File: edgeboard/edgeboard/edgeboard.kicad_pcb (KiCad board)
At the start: 2 copper layers, 117.2 x 150.2 mm, 26 parts

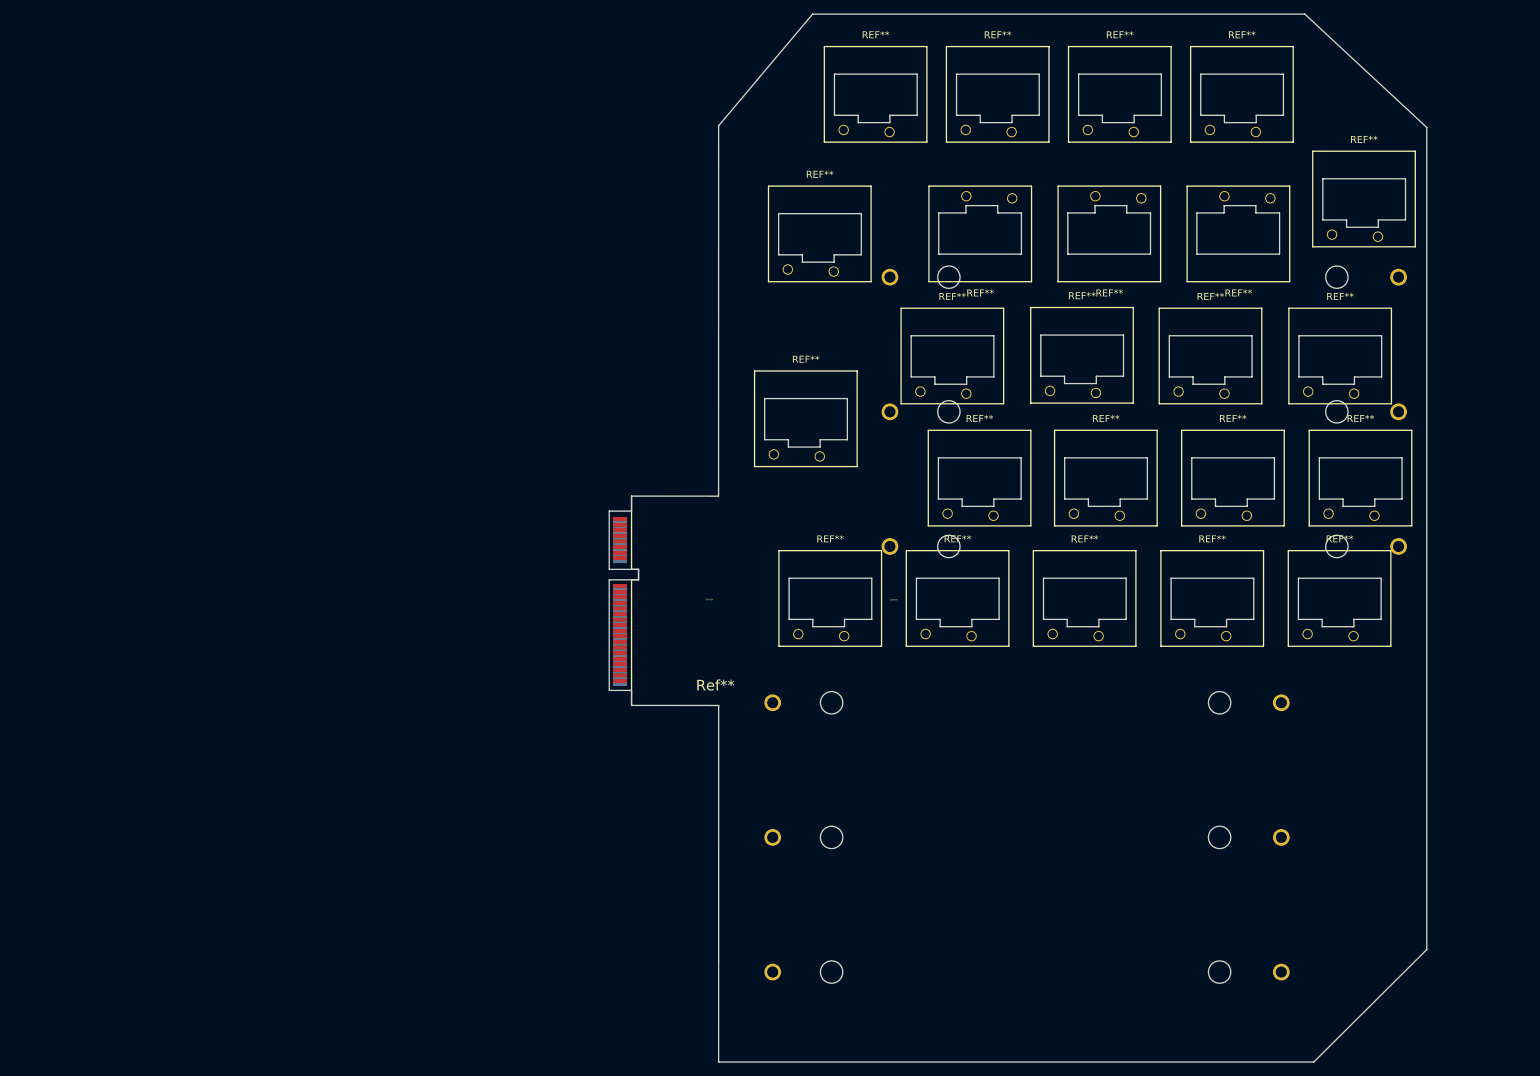
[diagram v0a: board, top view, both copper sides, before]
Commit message: added USB-C
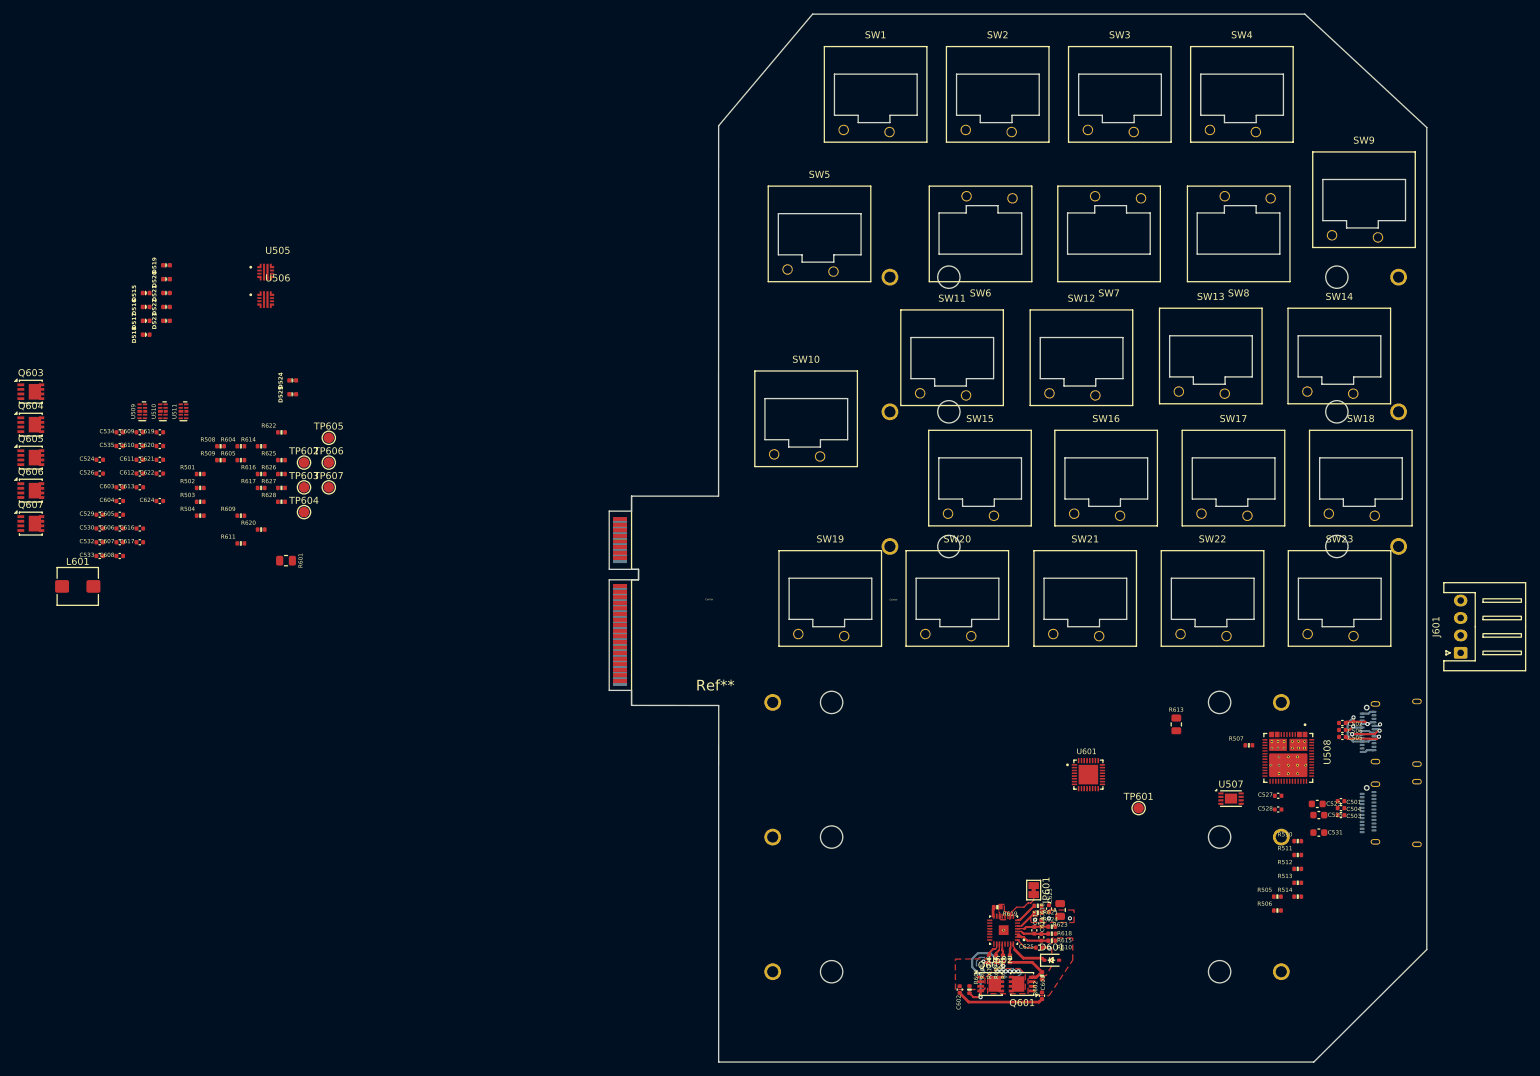
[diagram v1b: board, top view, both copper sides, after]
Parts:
- removed REF** (x16): SW_Kailh_Choc_Mini_1.00u, PCM_Switch_Keyboard_Kailh:SW_Kailh_Choc_Mini_1.00u
- removed REF** (x4): SW_Kailh_Choc_Mini_1.25u_90deg, PCM_Switch_Keyboard_Kailh:SW_Kailh_Choc_Mini_1.25u_90deg
- removed REF**: SW_Kailh_Choc_Mini_1.50u, PCM_Switch_Keyboard_Kailh:SW_Kailh_Choc_Mini_1.50u
- removed REF**: SW_Kailh_Choc_Mini_1.50u_90deg, PCM_Switch_Keyboard_Kailh:SW_Kailh_Choc_Mini_1.50u_90deg
- removed REF** (x2): BAT_BK-18650-PC6, keyswitch:BAT_BK-18650-PC6
- removed REF**: SW_Kailh_Choc_Mini_ISOEnter_180deg, PCM_Switch_Keyboard_Kailh:SW_Kailh_Choc_Mini_ISOEnter_180deg
- added BT1: BK-18650-PC6, keyswitch:BAT_BK-18650-PC6, B.Cu at (214.8, 69.0)
- added BT2: BK-18650-PC6, keyswitch:BAT_BK-18650-PC6, B.Cu at (198.0, 129.9)
- added C501: 100nF/50V, A_HDJ_Library:C_0402_1005Metric, F.Cu at (243.2, 124.8)
- added C502: 100nF/50V, A_HDJ_Library:C_0402_1005Metric, F.Cu at (243.4, 113.6)
- added C503: 47pF, A_HDJ_Library:C_0402_1005Metric, F.Cu at (243.2, 126.8)
- added C504: 47pF, A_HDJ_Library:C_0402_1005Metric, F.Cu at (243.2, 125.8)
- added C505: 47pF, A_HDJ_Library:C_0402_1005Metric, F.Cu at (243.4, 115.6)
- added C506: 47pF, A_HDJ_Library:C_0402_1005Metric, F.Cu at (243.4, 114.6)
- added C523: 22uF/10V, A_HDJ_Library:C_0603_1608Metric, F.Cu at (239.8, 125.2)
- added C524: 100nF/50V, A_HDJ_Library:C_0402_1005Metric, F.Cu at (65.3, 75.9)
- added C525: 10uF/10V, A_HDJ_Library:C_0603_1608Metric, F.Cu at (240.0, 126.8)
- added C526: 100nF/50V, A_HDJ_Library:C_0402_1005Metric, F.Cu at (65.3, 77.8)
- added C527: 100nF/50V, A_HDJ_Library:C_0402_1005Metric, F.Cu at (234.2, 124.0)
- added C528: 4.7uF/10V, A_HDJ_Library:C_0402_1005Metric, F.Cu at (234.2, 126.0)
- added C529: 47pF/50V, A_HDJ_Library:C_0402_1005Metric, F.Cu at (65.3, 83.8)
- added C530: 47pF/50V, A_HDJ_Library:C_0402_1005Metric, F.Cu at (65.3, 85.7)
- added C531: 10uF/10V, A_HDJ_Library:C_0603_1608Metric, F.Cu at (240.0, 129.3)
- added C532: 100nF/50V, A_HDJ_Library:C_0402_1005Metric, F.Cu at (65.3, 87.7)
- added C533: 100nF/50V, A_HDJ_Library:C_0402_1005Metric, F.Cu at (65.3, 89.7)
- added C534: 47pF/50V, A_HDJ_Library:C_0402_1005Metric, F.Cu at (68.2, 71.9)
- added C535: 47pF/50V, A_HDJ_Library:C_0402_1005Metric, F.Cu at (68.2, 73.9)
- added C601: 0.1u, A_HDJ_Library:C_0402_1005Metric, F.Cu at (200.3, 152.7)
- added C602: 0.1u, A_HDJ_Library:C_0402_1005Metric, F.Cu at (188.6, 151.8)
- added C603: 3x10uF MLCC, A_HDJ_Library:C_0402_1005Metric, F.Cu at (68.2, 79.8)
- added C604: 47n, A_HDJ_Library:C_0402_1005Metric, F.Cu at (68.2, 81.8)
- added C605: 47n, A_HDJ_Library:C_0402_1005Metric, F.Cu at (68.2, 83.8)
- added C606: 10uF MLCC, A_HDJ_Library:C_0402_1005Metric, F.Cu at (68.2, 85.7)
- added C607: 10uF MLCC, A_HDJ_Library:C_0402_1005Metric, F.Cu at (68.2, 87.7)
- added C608: 10uF MLCC, A_HDJ_Library:C_0402_1005Metric, F.Cu at (68.2, 89.7)
- added C609: 10uF MLCC, A_HDJ_Library:C_0402_1005Metric, F.Cu at (71.0, 71.9)
- added C610: 33n, A_HDJ_Library:C_0402_1005Metric, F.Cu at (71.0, 73.9)
- added C611: 33n, A_HDJ_Library:C_0402_1005Metric, F.Cu at (71.0, 75.9)
- added C612: 0.47u, A_HDJ_Library:C_0402_1005Metric, F.Cu at (71.0, 77.8)
- added C613: 0.1u, A_HDJ_Library:C_0402_1005Metric, F.Cu at (71.0, 79.8)
- added C614: 0.1u, A_HDJ_Library:C_0402_1005Metric, F.Cu at (200.2, 144.3)
- added C615: 0.1u, A_HDJ_Library:C_0402_1005Metric, F.Cu at (199.2, 143.3)
- added C616: 33p, A_HDJ_Library:C_0402_1005Metric, F.Cu at (71.0, 85.7)
- added C617: 1800p, A_HDJ_Library:C_0402_1005Metric, F.Cu at (71.0, 87.7)
- added C618: 0.1u, A_HDJ_Library:C_0402_1005Metric, F.Cu at (200.2, 142.3)
- added C619: 1u, A_HDJ_Library:C_0402_1005Metric, F.Cu at (73.9, 71.9)
- added C620: 2.2u, A_HDJ_Library:C_0402_1005Metric, F.Cu at (73.9, 73.9)
- added C621: 15p, A_HDJ_Library:C_0402_1005Metric, F.Cu at (73.9, 75.9)
- added C622: 680p, A_HDJ_Library:C_0402_1005Metric, F.Cu at (73.9, 77.8)
- added C623: 0.1u, A_HDJ_Library:C_0402_1005Metric, F.Cu at (201.3, 140.2)
- added C624: 100p, A_HDJ_Library:C_0402_1005Metric, F.Cu at (73.9, 81.8)
- added C625: 2.2u, A_HDJ_Library:C_0402_1005Metric, F.Cu at (199.9, 145.8)
- added D515: ESD9B3.3ST5GOSCT-ND, A_HDJ_Library:D_0402_1005Metric, F.Cu at (72.0, 52.0)
- added D516: ESD9B3.3ST5GOSCT-ND, A_HDJ_Library:D_0402_1005Metric, F.Cu at (72.0, 54.0)
- added D517: ESD9B3.3ST5GOSCT-ND, A_HDJ_Library:D_0402_1005Metric, F.Cu at (72.0, 56.0)
- added D518: ESD9B3.3ST5GOSCT-ND, A_HDJ_Library:D_0402_1005Metric, F.Cu at (72.0, 57.9)
- added D519: ESD9B3.3ST5GOSCT-ND, A_HDJ_Library:D_0402_1005Metric, F.Cu at (74.9, 48.0)
- added D520: ESD9B3.3ST5GOSCT-ND, A_HDJ_Library:D_0402_1005Metric, F.Cu at (74.9, 50.0)
- added D521: ESD9B3.3ST5GOSCT-ND, A_HDJ_Library:D_0402_1005Metric, F.Cu at (74.9, 52.0)
- added D522: ESD9B3.3ST5GOSCT-ND, A_HDJ_Library:D_0402_1005Metric, F.Cu at (74.9, 54.0)
- added D523: ESD9B3.3ST5GOSCT-ND, A_HDJ_Library:D_0402_1005Metric, F.Cu at (74.9, 56.0)
- added D524: ESD9B3.3ST5GOSCT-ND, A_HDJ_Library:D_0402_1005Metric, F.Cu at (93.0, 64.5)
- added D525: ESD9B3.3ST5GOSCT-ND, A_HDJ_Library:D_0402_1005Metric, F.Cu at (93.0, 66.5)
- added D601: BAT54HT1, A_HDJ_Library:D_SOD-323, F.Cu at (201.8, 147.6)
- added J501: USB_C_Receptacle, Connector_USB:USB_C_Receptacle_Amphenol_12401610E4-2A, B.Cu at (251.2, 126.5)
- added J502: USB_C_Receptacle, Connector_USB:USB_C_Receptacle_Amphenol_12401610E4-2A, B.Cu at (251.2, 115.0)
- added J601: JST XH 4 pin, Connector_JST:JST_XH_S4B-XH-A_1x04_P2.50mm_Horizontal, F.Cu at (260.4, 103.5)
- added JP601: Jumper_2_Bridged, Jumper:SolderJumper-2_P1.3mm_Bridged_Pad1.0x1.5mm, F.Cu at (199.2, 137.6)
- added L601: 2.2uH 4.5A+, Inductor_SMD:L_Bourns_SRP5030T, F.Cu at (62.1, 94.0)
- added Q601: CSD17551Q3A, Package_SO:Vishay_PowerPAK_1212-8_Single, F.Cu at (197.5, 151.0)
- added Q602: CSD17551Q3A, Package_SO:Vishay_PowerPAK_1212-8_Single, F.Cu at (193.0, 151.0)
- added Q603: CSD17551Q3A, Package_SO:Vishay_PowerPAK_1212-8_Single, F.Cu at (55.4, 66.1)
- added Q604: CSD17551Q3A, Package_SO:Vishay_PowerPAK_1212-8_Single, F.Cu at (55.4, 70.8)
- added Q605: CSD17551Q3A, Package_SO:Vishay_PowerPAK_1212-8_Single, F.Cu at (55.4, 75.6)
- added Q606: CSD17551Q3A, Package_SO:Vishay_PowerPAK_1212-8_Single, F.Cu at (55.4, 80.3)
- added Q607: CSD25402Q3A, Package_SO:Vishay_PowerPAK_1212-8_Single, F.Cu at (55.4, 85.0)
- added R501: 100K/1%, A_HDJ_Library:R_0402_1005Metric, F.Cu at (79.7, 77.9)
- added R502: 100K/1%, A_HDJ_Library:R_0402_1005Metric, F.Cu at (79.7, 79.9)
- added R503: 100K/1%, A_HDJ_Library:R_0402_1005Metric, F.Cu at (79.7, 81.9)
- added R504: 100K/1%, A_HDJ_Library:R_0402_1005Metric, F.Cu at (79.7, 83.9)
- added R505: 10K/1%, A_HDJ_Library:R_0402_1005Metric, F.Cu at (234.1, 138.5)
- added R506: 10K/1%, A_HDJ_Library:R_0402_1005Metric, F.Cu at (234.1, 140.5)
- added R507: 100K, A_HDJ_Library:R_0402_1005Metric, F.Cu at (230.0, 116.8)
- added R508: 100K/1%, A_HDJ_Library:R_0402_1005Metric, F.Cu at (82.6, 73.9)
- added R509: 100K/1%, A_HDJ_Library:R_0402_1005Metric, F.Cu at (82.6, 75.9)
- added R510: 100K/1%, A_HDJ_Library:R_0402_1005Metric, F.Cu at (237.0, 130.5)
- added R511: 100K/1%, A_HDJ_Library:R_0402_1005Metric, F.Cu at (237.0, 132.5)
- added R512: 100K/1%, A_HDJ_Library:R_0402_1005Metric, F.Cu at (237.0, 134.5)
- added R513: 10K, A_HDJ_Library:R_0402_1005Metric, F.Cu at (237.0, 136.5)
- added R514: 19.1K/1%, A_HDJ_Library:R_0402_1005Metric, F.Cu at (237.0, 138.5)
- added R601: 10m, A_HDJ_Library:R_0805_2012Metric, F.Cu at (92.0, 90.3)
- added R602: 10M, A_HDJ_Library:R_0402_1005Metric, F.Cu at (200.3, 149.8)
- added R603: 10M, A_HDJ_Library:R_0402_1005Metric, F.Cu at (189.9, 151.8)
- added R604: 4.99, A_HDJ_Library:R_0402_1005Metric, F.Cu at (85.5, 73.9)
- added R605: 4.99, A_HDJ_Library:R_0402_1005Metric, F.Cu at (85.5, 75.9)
- added R606: 5.1k, A_HDJ_Library:R_0402_1005Metric, F.Cu at (195.8, 147.4)
- added R607: 5.1k, A_HDJ_Library:R_0402_1005Metric, F.Cu at (194.8, 147.4)
- added R608: 100, A_HDJ_Library:R_0402_1005Metric, F.Cu at (192.8, 147.4)
- added R609: 1, A_HDJ_Library:R_0402_1005Metric, F.Cu at (85.5, 83.9)
- added R610: 100, A_HDJ_Library:R_0402_1005Metric, F.Cu at (201.8, 144.8)
- added R611: 10, A_HDJ_Library:R_0402_1005Metric, F.Cu at (85.5, 87.9)
- added R612: 10K, A_HDJ_Library:R_0402_1005Metric, F.Cu at (193.8, 147.4)
- added R613: 10m, A_HDJ_Library:R_0805_2012Metric, F.Cu at (219.6, 113.8)
- added R614: 10, A_HDJ_Library:R_0402_1005Metric, F.Cu at (88.4, 73.9)
- added R615: 100, A_HDJ_Library:R_0402_1005Metric, F.Cu at (201.8, 143.8)
- added R616: 40.2k, A_HDJ_Library:R_0402_1005Metric, F.Cu at (88.4, 77.9)
- added R617: 10, A_HDJ_Library:R_0402_1005Metric, F.Cu at (88.4, 79.9)
- added R618: 100, A_HDJ_Library:R_0402_1005Metric, F.Cu at (201.8, 142.8)
- added R619: 10K, A_HDJ_Library:R_0402_1005Metric, F.Cu at (193.9, 140.0)
- added R620: 10k, A_HDJ_Library:R_0402_1005Metric, F.Cu at (88.4, 85.9)
- added R621: 100, A_HDJ_Library:R_0402_1005Metric, F.Cu at (199.8, 139.8)
- added R622: TBD, A_HDJ_Library:R_0402_1005Metric, F.Cu at (91.3, 71.9)
- added R623: 0.001, A_HDJ_Library:R_0805_2012Metric, F.Cu at (202.9, 140.4)
- added R624: 100, A_HDJ_Library:R_0402_1005Metric, F.Cu at (199.8, 140.8)
- added R625: TBD, A_HDJ_Library:R_0402_1005Metric, F.Cu at (91.3, 75.9)
- added R626: TBD, A_HDJ_Library:R_0402_1005Metric, F.Cu at (91.3, 77.9)
- added R627: 137K, A_HDJ_Library:R_0402_1005Metric, F.Cu at (91.3, 79.9)
- added R628: TBD, A_HDJ_Library:R_0402_1005Metric, F.Cu at (91.3, 81.9)
- added SW1: SW_Push, PCM_Switch_Keyboard_Kailh:SW_Kailh_Choc_Mini_1.25u_90deg, F.Cu at (176.5, 23.5)
- added SW10: SW_Push, PCM_Switch_Keyboard_Kailh:SW_Kailh_Choc_Mini_ISOEnter_180deg, F.Cu at (166.5, 70.0)
- added SW11: SW_Push, PCM_Switch_Keyboard_Kailh:SW_Kailh_Choc_Mini_1.00u, F.Cu at (187.5, 61.2)
- added SW12: SW_Push, PCM_Switch_Keyboard_Kailh:SW_Kailh_Choc_Mini_1.00u, F.Cu at (206.0, 61.2)
- added SW13: SW_Push, PCM_Switch_Keyboard_Kailh:SW_Kailh_Choc_Mini_1.00u, F.Cu at (224.5, 61.0)
- added SW14: SW_Push, PCM_Switch_Keyboard_Kailh:SW_Kailh_Choc_Mini_1.00u, F.Cu at (243.0, 61.0)
- added SW15: SW_Push, PCM_Switch_Keyboard_Kailh:SW_Kailh_Choc_Mini_1.00u, F.Cu at (191.5, 78.5)
- added SW16: SW_Push, PCM_Switch_Keyboard_Kailh:SW_Kailh_Choc_Mini_1.00u, F.Cu at (209.5, 78.5)
- added SW17: SW_Push, PCM_Switch_Keyboard_Kailh:SW_Kailh_Choc_Mini_1.00u, F.Cu at (227.8, 78.5)
- added SW18: SW_Push, PCM_Switch_Keyboard_Kailh:SW_Kailh_Choc_Mini_1.00u, F.Cu at (246.0, 78.5)
- added SW19: SW_Push, PCM_Switch_Keyboard_Kailh:SW_Kailh_Choc_Mini_1.00u, F.Cu at (170.0, 95.8)
- added SW2: SW_Push, PCM_Switch_Keyboard_Kailh:SW_Kailh_Choc_Mini_1.25u_90deg, F.Cu at (194.0, 23.5)
- added SW20: SW_Push, PCM_Switch_Keyboard_Kailh:SW_Kailh_Choc_Mini_1.00u, F.Cu at (188.2, 95.8)
- added SW21: SW_Push, PCM_Switch_Keyboard_Kailh:SW_Kailh_Choc_Mini_1.00u, F.Cu at (206.5, 95.8)
- added SW22: SW_Push, PCM_Switch_Keyboard_Kailh:SW_Kailh_Choc_Mini_1.00u, F.Cu at (224.8, 95.8)
- added SW23: SW_Push, PCM_Switch_Keyboard_Kailh:SW_Kailh_Choc_Mini_1.00u, F.Cu at (243.0, 95.8)
- added SW3: SW_Push, PCM_Switch_Keyboard_Kailh:SW_Kailh_Choc_Mini_1.25u_90deg, F.Cu at (211.5, 23.5)
- added SW4: SW_Push, PCM_Switch_Keyboard_Kailh:SW_Kailh_Choc_Mini_1.25u_90deg, F.Cu at (229.0, 23.5)
- added SW5: SW_Push, PCM_Switch_Keyboard_Kailh:SW_Kailh_Choc_Mini_1.50u, F.Cu at (168.5, 43.5)
- added SW6: SW_Push, PCM_Switch_Keyboard_Kailh:SW_Kailh_Choc_Mini_1.00u, F.Cu at (191.5, 43.5)
- added SW7: SW_Push, PCM_Switch_Keyboard_Kailh:SW_Kailh_Choc_Mini_1.00u, F.Cu at (210.0, 43.5)
- added SW8: SW_Push, PCM_Switch_Keyboard_Kailh:SW_Kailh_Choc_Mini_1.00u, F.Cu at (228.5, 43.5)
- added SW9: SW_Push, PCM_Switch_Keyboard_Kailh:SW_Kailh_Choc_Mini_1.50u_90deg, F.Cu at (246.5, 38.6)
- added TP601: VBAT, TestPoint:TestPoint_Pad_D1.5mm, F.Cu at (214.2, 125.8)
- added TP602: VCHARGE, TestPoint:TestPoint_Pad_D1.5mm, F.Cu at (94.6, 76.3)
- added TP603: VSYSTEM, TestPoint:TestPoint_Pad_D1.5mm, F.Cu at (94.6, 79.8)
- added TP604: PSYS, TestPoint:TestPoint_Pad_D1.5mm, F.Cu at (94.6, 83.4)
- added TP605: PROCHOT, TestPoint:TestPoint_Pad_D1.5mm, F.Cu at (98.1, 72.7)
- added TP606: IBAT, TestPoint:TestPoint_Pad_D1.5mm, F.Cu at (98.1, 76.3)
- added TP607: CHRG_OK, TestPoint:TestPoint_Pad_D1.5mm, F.Cu at (98.1, 79.8)
- added U505: LM73100RPWR, ComputemanParts:IC_LM73100RPWR, F.Cu at (89.1, 49.0)
- added U506: LM73100RPWR, ComputemanParts:IC_LM73100RPWR, F.Cu at (89.1, 52.9)
- added U507: AT25DN512C-MAHF-T, Package_DFN_QFN:DFN-8-1EP_3x2mm_P0.5mm_EP1.75x1.45mm, F.Cu at (227.4, 124.4)
- added U508: TPS65988DHRSHR, ComputemanParts:IC_TPS65987DDHRSHR, F.Cu at (235.7, 118.6)
- added U509: ULC0524P, A_HDJ_Library:Diodes_UDFN-10_1.0x2.5mm_P0.5mm, F.Cu at (71.4, 68.9)
- added U510: ULC0524P, A_HDJ_Library:Diodes_UDFN-10_1.0x2.5mm_P0.5mm, F.Cu at (74.3, 68.9)
- added U511: ULC0524P, A_HDJ_Library:Diodes_UDFN-10_1.0x2.5mm_P0.5mm, F.Cu at (77.3, 68.9)
- added U601: BQ25710RSNT, ComputemanParts:QFN40P400X400X80-33N, F.Cu at (207.0, 121.0)
- added U602: BQ40Z50RSMR-R2, ComputemanParts:QFN40P400X400X100-33N, F.Cu at (194.8, 143.3)
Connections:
- net GPIO2 renamed GPIO_2
- Ref** pad 1: (no net) -> SMB_DATA
- Ref** pad 17: (no net) -> GND
- Ref** pad 18: (no net) -> GND
- Ref** pad 19: (no net) -> GND
- Ref** pad 20: (no net) -> GND
- Ref** pad 21: (no net) -> GND
- Ref** pad 22: (no net) -> GND
- Ref** pad 23: (no net) -> GND
- Ref** pad 24: (no net) -> GND
- Ref** pad 25: (no net) -> GND
- Ref** pad 26: (no net) -> GND
- Ref** pad 27: (no net) -> GND
- Ref** pad 29: (no net) -> GND
- Ref** pad 3: (no net) -> SMB_CLK
- Ref** pad 38: (no net) -> +12v
- Ref** pad 39: (no net) -> +12v
- Ref** pad 40: (no net) -> +12v
- Ref** pad 41: (no net) -> +12v
- Ref** pad 42: (no net) -> +12v
- Ref** pad 43: (no net) -> +12v
- Ref** pad 44: (no net) -> +12v
- Ref** pad 45: (no net) -> +12v
- Ref** pad 46: (no net) -> +12v
- Ref** pad 47: (no net) -> +12v
- Ref** pad 48: (no net) -> +12v
- Ref** pad 49: (no net) -> +12v
- Ref** pad 5: (no net) -> SMB_ALERT
- Ref** pad 50: (no net) -> +12v
- Ref** pad 51: (no net) -> +12v
- Ref** pad 52: (no net) -> +12v
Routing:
- net Net-(Q602-G): track 0.00 -> 14.8 mm, vias 0 -> 2
- net /USBC2_VBUS: track 0.00 -> 13.0 mm, vias 0 -> 2
- net Net-(C601-Pad2): track 0.00 -> 12.5 mm
- net Net-(Q601-G): track 0.00 -> 6.88 mm
- net /USBC2_USB2_D-: track 0.00 -> 6.51 mm, vias 0 -> 2
- net Net-(D601-K): track 0.00 -> 5.80 mm
- net /USBC2_CC2: track 0.00 -> 5.74 mm, vias 0 -> 1
- net Net-(U602-VC3): track 0.00 -> 5.35 mm
- net Net-(JP601-B): track 0.00 -> 5.31 mm
- net GND: track 0.00 -> 4.77 mm, vias 0 -> 4
- net Net-(U602-VC2): track 0.00 -> 4.56 mm
- net Net-(U602-VC1): track 0.00 -> 4.52 mm
- net Net-(Q601-D): track 0.00 -> 3.85 mm, vias 0 -> 7
- net Net-(U602-SRP): track 0.00 -> 3.24 mm
- net Net-(U602-SRN): track 0.00 -> 3.21 mm
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- added copper zone on F.Cu, net /PACK+
- added copper zone on F.Cu, net /VBAT
- added copper zone on F.Cu, net GND
- added copper zone on B.Cu, net Net-(Q601-D)
- added copper zone on F.Cu, net Net-(Q601-D)
